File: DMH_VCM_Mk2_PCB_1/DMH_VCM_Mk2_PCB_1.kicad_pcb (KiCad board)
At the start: 2 copper layers, 48 x 175 mm, 88 parts, among them J1 TS_Jack_6.35mm_Sw, J10 TS_Jack_6.35mm_Sw, J100 IDC_02x05, J2 TS_Jack_6.35mm_Sw, J200 IDC_02x05, J3 TS_Jack_6.35mm_Sw, J4 TS_Jack_6.35mm_Sw, J5 TS_Jack_6.35mm_Sw, J50 Conn_01x06, J6 TS_Jack_6.35mm_Sw, J60 Conn_01x06, J7 TS_Jack_6.35mm_Sw, J70 Conn_01x06, J8 TS_Jack_6.35mm_Sw, J9 TS_Jack_6.35mm_Sw, Q1 BC548, Q2 BC548, Q3 BC548, Q4 BC548, Q5 BC548, Q6 BC548, U1 TL074, U2 TL074

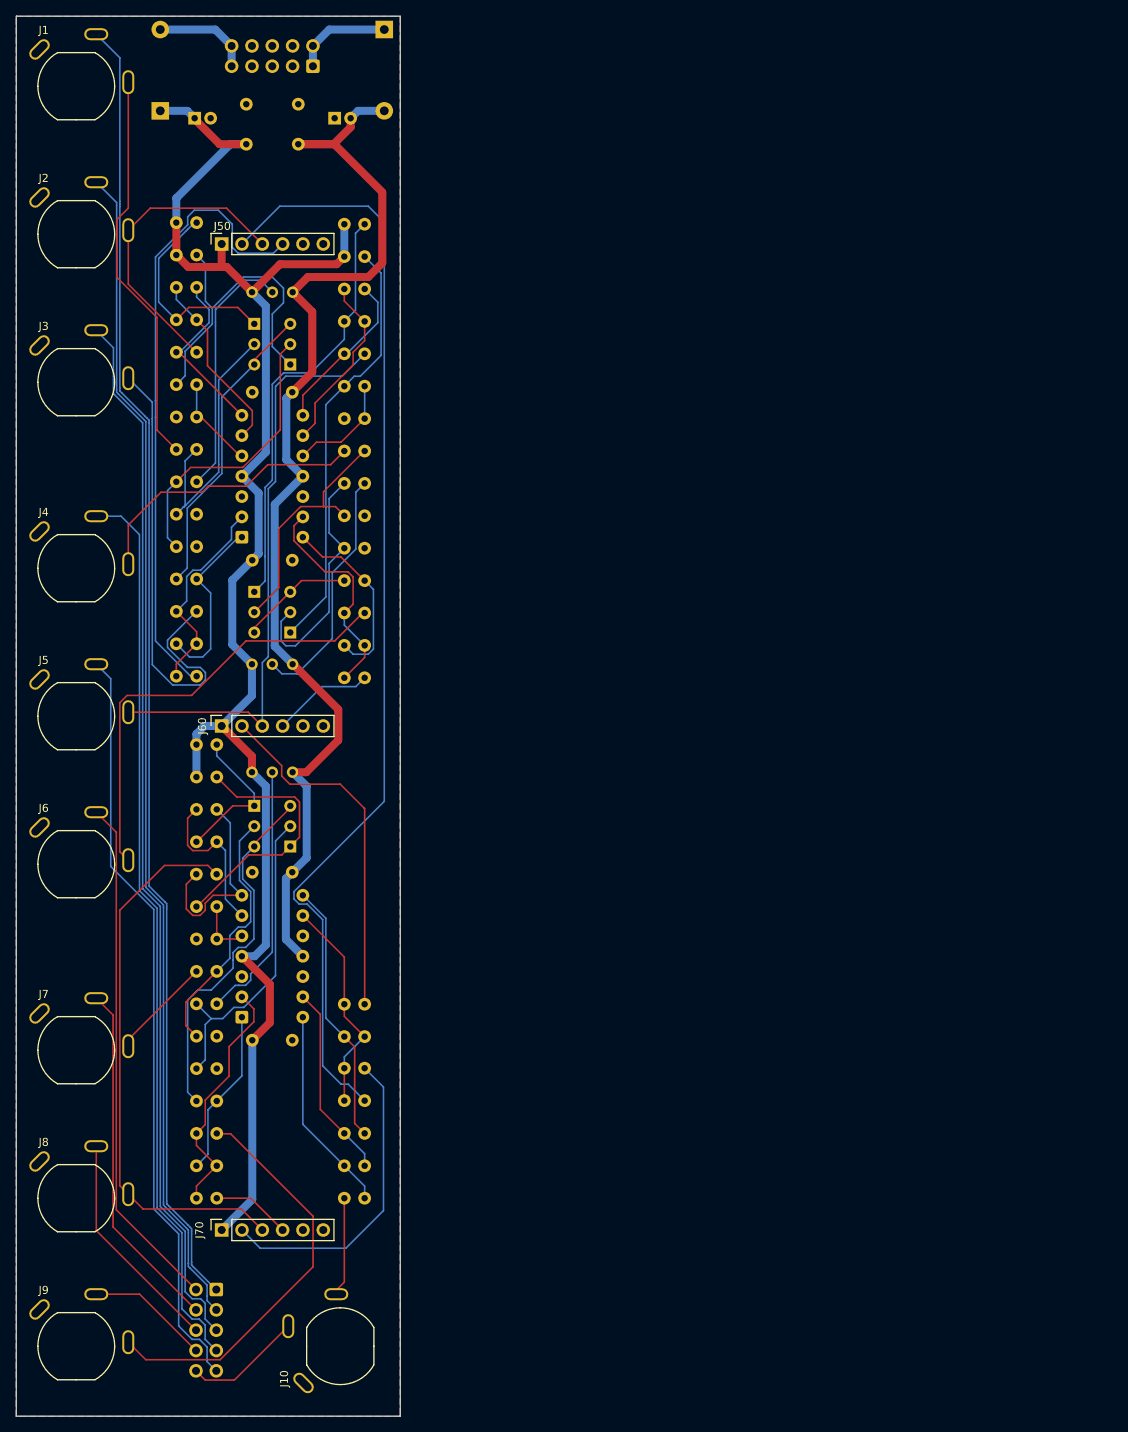
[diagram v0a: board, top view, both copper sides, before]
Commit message: PCB 1 placement in progress
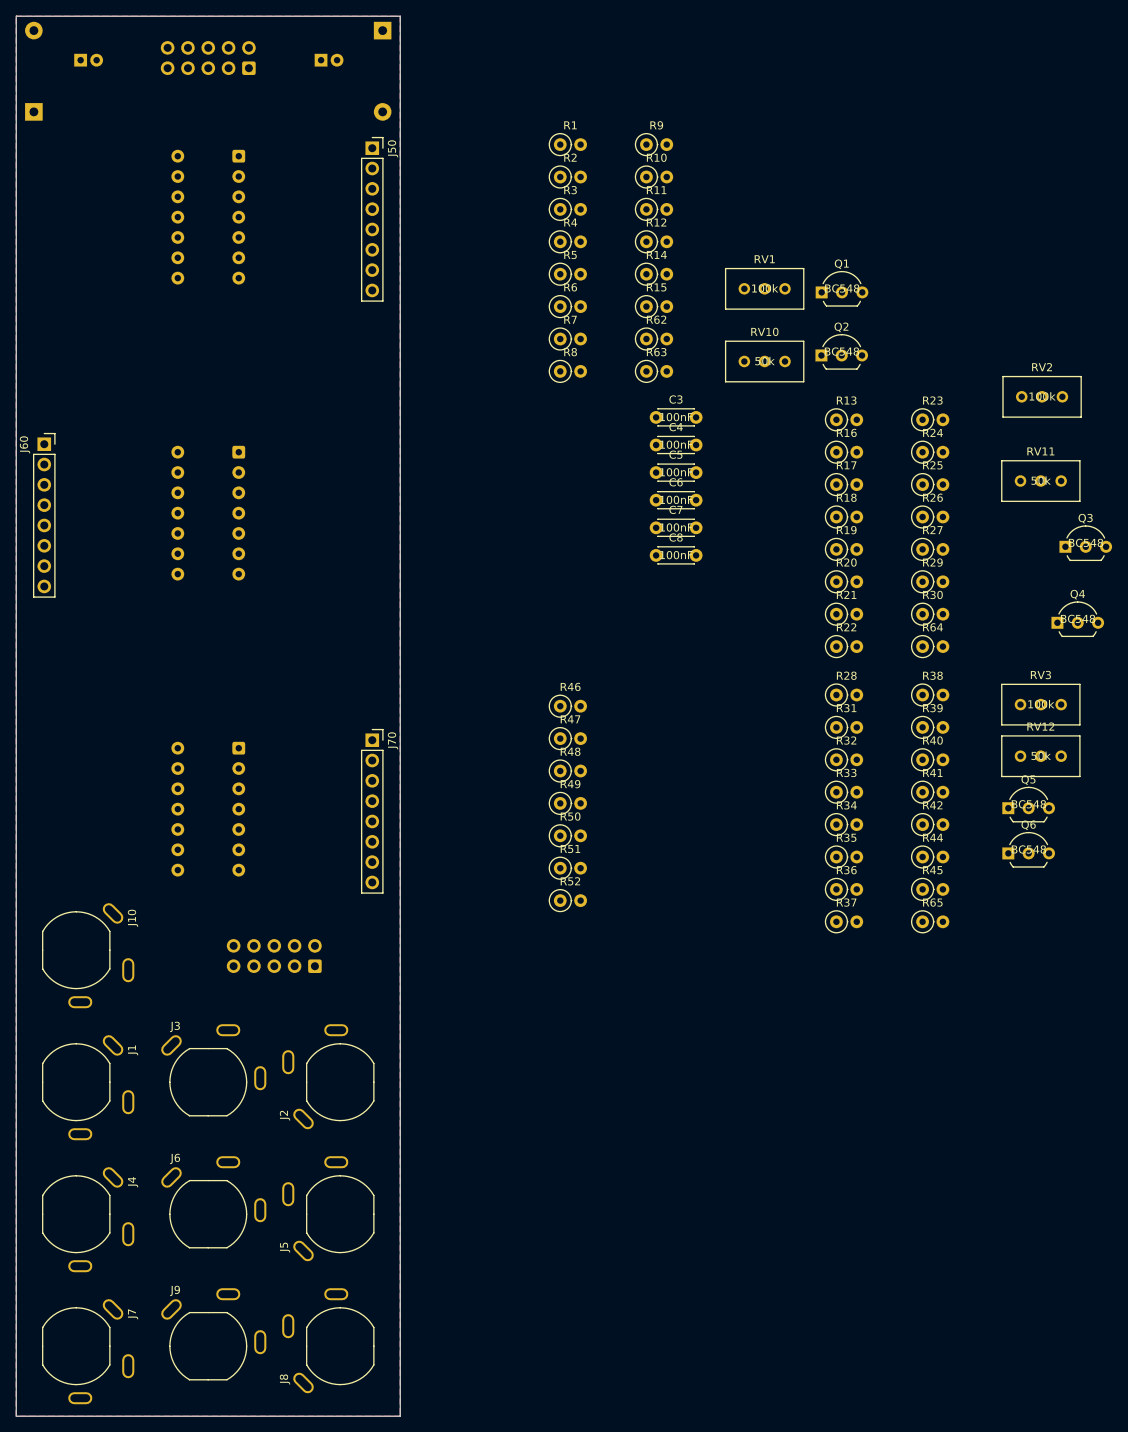
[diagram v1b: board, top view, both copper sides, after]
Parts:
- removed R43: 100k, Resistor_THT:R_Axial_DIN0207_L6.3mm_D2.5mm_P2.54mm_Vertical
- added R62: 33k, Resistor_THT:R_Axial_DIN0207_L6.3mm_D2.5mm_P2.54mm_Vertical, F.Cu at (129.8, 82.8)
- added R63: 100k, Resistor_THT:R_Axial_DIN0207_L6.3mm_D2.5mm_P2.54mm_Vertical, F.Cu at (129.8, 86.9)
- added R64: 100k, Resistor_THT:R_Axial_DIN0207_L6.3mm_D2.5mm_P2.54mm_Vertical, F.Cu at (164.3, 121.3)
- added R65: 100k, Resistor_THT:R_Axial_DIN0207_L6.3mm_D2.5mm_P2.54mm_Vertical, F.Cu at (164.3, 155.7)
- added RV10: 50k, Potentiometer_THT:Potentiometer_Bourns_3296W_Vertical, F.Cu at (147.1, 85.7)
- added RV11: 50k, Potentiometer_THT:Potentiometer_Bourns_3296W_Vertical, F.Cu at (181.6, 100.6)
- added RV12: 50k, Potentiometer_THT:Potentiometer_Bourns_3296W_Vertical, F.Cu at (181.6, 135.0)
- added U3: TL074, Package_DIP:DIP-14_W7.62mm_Socket, B.Cu at (78.8, 134.0)
- C3, C4, C5, C6, C7, C8, Q1, Q2, Q3, Q4, Q5, Q6, R1, R10, R11, R12, R14, R15, R16, R17, R18, R19, R2, R20, R21, R22, R23, R24, R25, R26, R27, R29, R3, R30, R31, R32, R33, R34, R35, R36, R37, R38, R39, R4, R40, R41, R42, R44, R45, R46, R47, R48, R49, R5, R50, R51, R52, R6, R7, R8, R9, RV1, RV2, RV3: moved to F.Cu
- J50, J60, J70: value Conn_01x06 -> Conn_01x08; footprint Connector_PinSocket_2.54mm:PinSocket_1x06_P2.54mm_Vertical -> Connector_PinSocket_2.54mm:PinSocket_1x08_P2.54mm_Vertical
- R13, R28: value 100k -> 33k; moved to F.Cu
- moved J1 124.5 mm to (58.5, 175.8), turned to -90 degrees
- moved J2 111.0 mm to (91.5, 175.8), turned to 90 degrees
- moved RV2 101.9 mm to (181.8, 90.1)
- moved Q3 101.6 mm to (182.1, 108.8), turned to 0 degrees
- moved RV3 96.4 mm to (181.6, 128.6)
- moved R44 96.3 mm to (164.3, 147.6), turned to 0 degrees
- moved R45 96.3 mm to (164.3, 151.7), turned to 0 degrees
- moved Q4 95.9 mm to (181.1, 118.3), turned to 0 degrees
- moved R38 94.8 mm to (164.3, 127.3), turned to 0 degrees
- moved R39 94.8 mm to (164.3, 131.4), turned to 0 degrees
- moved R40 94.8 mm to (164.3, 135.4), turned to 0 degrees
- moved R41 94.8 mm to (164.3, 139.5), turned to 0 degrees
- moved R42 94.8 mm to (164.3, 143.6), turned to 0 degrees
- moved Q5 94.3 mm to (175.0, 141.5), turned to 0 degrees
- moved Q6 89.8 mm to (175.0, 147.2), turned to 0 degrees
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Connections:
- J50 pad 5: GND -> /Inputs and Outputs/CV Amt A Pot
- J50 pad 6: GND -> /Inputs and Outputs/CV A Jack
- J60 pad 5: GND -> /Inputs and Outputs/CV Amt B Pot
- J60 pad 6: GND -> /Inputs and Outputs/CV B Jack
- J70 pad 5: GND -> /Inputs and Outputs/CV Amt C Pot
- J70 pad 6: GND -> /Inputs and Outputs/CV C Jack
- R13 pad 1: /Inputs and Outputs/CV A Jack -> /Inputs and Outputs/CV B Jack
- R13 pad 2: Net-(U1A--) -> Net-(U2D--)
- R18 pad 2: Net-(U1C--) -> Net-(U2A--)
- R19 pad 1: Net-(U1C--) -> Net-(U2A--)
- R21 pad 1: Net-(U1C-+) -> Net-(U2A-+)
- R22 pad 1: Net-(U1C-+) -> Net-(U2A-+)
- R28 pad 1: /Inputs and Outputs/CV B Jack -> /Inputs and Outputs/CV C Jack
- R28 pad 2: Net-(U1D--) -> Net-(U3A--)
- R29 pad 1: Net-(U1D--) -> Net-(U1C--)
- R3 pad 2: Net-(U1B--) -> Net-(U1D--)
- R30 pad 2: Net-(U1D--) -> Net-(U1C--)
- R33 pad 2: Net-(U2B--) -> Net-(U3B--)
- R34 pad 1: Net-(U2B--) -> Net-(U3B--)
- R36 pad 1: Net-(U2B-+) -> Net-(U3B-+)
- R37 pad 1: Net-(U2B-+) -> Net-(U3B-+)
- R4 pad 1: Net-(U1B--) -> Net-(U1D--)
- R44 pad 1: Net-(U2A--) -> Net-(U2B--)
- R45 pad 2: Net-(U2A--) -> Net-(U2B--)
- R46 pad 2: Net-(U2C--) -> Net-(U3D--)
- R47 pad 1: Net-(U2C--) -> Net-(U3D--)
- R48 pad 2: Net-(U2C--) -> Net-(U3D--)
- R49 pad 2: Net-(U2C--) -> Net-(U3D--)
- R50 pad 2: Net-(U2D--) -> Net-(U3C--)
- R51 pad 1: Net-(U2D--) -> Net-(U3C--)
- R6 pad 1: Net-(U1B-+) -> Net-(U1D-+)
- R7 pad 1: Net-(U1B-+) -> Net-(U1D-+)
- U1 pad 10: Net-(U1C-+) -> GND
- U1 pad 12: GND -> Net-(U1D-+)
- U1 pad 14: Net-(R27-Pad1) -> Net-(R3-Pad1)
- U1 pad 5: Net-(U1B-+) -> /Inputs and Outputs/CV Amt A Pot
- U1 pad 7: Net-(R3-Pad1) -> Net-(R63-Pad1)
- U1 pad 8: Net-(R18-Pad1) -> Net-(R27-Pad1)
- U2 pad 1: Net-(R42-Pad1) -> Net-(R18-Pad1)
- U2 pad 12: GND -> /Inputs and Outputs/CV Amt B Pot
- U2 pad 14: Net-(R51-Pad2) -> Net-(R64-Pad1)
- U2 pad 3: GND -> Net-(U2A-+)
- U2 pad 5: Net-(U2B-+) -> GND
- U2 pad 7: Net-(R33-Pad1) -> Net-(R42-Pad1)
- U2 pad 8: Net-(R47-Pad2) -> Net-(U2C--)
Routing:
- net +12V: track 204.9 -> 0.00 mm
- net Net-(J200-Pin_1): track 163.2 -> 0.00 mm
- net Net-(J200-Pin_2): track 147.2 -> 0.00 mm
- net -12V: track 144.7 -> 0.00 mm
- net /Inputs and Outputs/Mute A Switch: track 139.8 -> 0.00 mm
- net Net-(J200-Pin_3): track 131.8 -> 0.00 mm
- net Net-(J200-Pin_4): track 112.8 -> 0.00 mm
- net Net-(J200-Pin_5): track 95.1 -> 0.00 mm
- net /Inputs and Outputs/Offset A Pot: track 78.3 -> 0.00 mm
- net /Inputs and Outputs/Output B Jack: track 73.4 -> 0.00 mm
- net /Inputs and Outputs/Output C Jack: track 69.4 -> 0.00 mm
- net Net-(J200-Pin_6): track 64.8 -> 0.00 mm
- net /Inputs and Outputs/CV A Jack: track 58.0 -> 0.00 mm
- net /Inputs and Outputs/CV B Jack: track 55.4 -> 0.00 mm
- net Net-(Q3-C): track 53.7 -> 0.00 mm
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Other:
- board text added: "Mk2.0 - Month 2025"
- board text removed: "Mk1.1 - March 2025"

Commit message: PCB 1 placement done
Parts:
- C3, C4, C5, C6, C7, C8, Q1, Q2, Q3, Q4, Q5, Q6, R1, R10, R11, R12, R13, R14, R15, R16, R17, R18, R19, R2, R20, R21, R22, R23, R24, R25, R26, R27, R28, R29, R3, R30, R31, R32, R33, R34, R35, R36, R37, R38, R39, R4, R40, R41, R42, R44, R45, R46, R47, R48, R49, R5, R50, R51, R52, R6, R62, R63, R64, R65, R7, R8, R9, RV1, RV10, RV11, RV12, RV2, RV3: moved to B.Cu
- moved RV3 117.9 mm to (63.7, 129.5), turned to 180 degrees
- moved RV2 116.3 mm to (65.5, 92.5)
- moved RV11 116.1 mm to (65.5, 98.0)
- moved R64 102.5 mm to (69.8, 81.5), turned to 180 degrees
- moved R30 102.1 mm to (69.8, 78.5), turned to 180 degrees
- moved Q2 101.4 mm to (52.7, 62.8)
- moved R29 100.8 mm to (67.7, 84.5)
- moved R27 99.0 mm to (67.7, 87.5)
- moved RV12 98.5 mm to (83.2, 129.8), turned to -90 degrees
- moved Q1 95.6 mm to (57.8, 59.0), turned to 180 degrees
- moved R65 95.1 mm to (82.7, 106.8)
- moved R45 91.7 mm to (82.7, 109.8)
- moved Q4 90.7 mm to (92.2, 100.7)
- moved R44 88.7 mm to (82.7, 112.8)
- moved R42 86.2 mm to (82.7, 115.8)
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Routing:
- net Net-(D2-K): track 0.00 -> 17.6 mm
- net Net-(D1-A): track 0.00 -> 17.6 mm

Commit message: PCB 1 routine in progress
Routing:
- net +12V: track 0.00 -> 202.2 mm
- net -12V: track 0.00 -> 157.2 mm
- net /Inputs and Outputs/Mute A Switch: track 0.00 -> 155.9 mm
- net /Inputs and Outputs/CV B Jack: track 0.00 -> 152.4 mm
- net /Inputs and Outputs/Output A Jack: track 0.00 -> 144.0 mm
- net /Inputs and Outputs/Input B Jack: track 0.00 -> 119.8 mm
- net /Inputs and Outputs/Input A Jack: track 0.00 -> 113.9 mm
- net Net-(Q1-B): track 0.00 -> 54.3 mm
- net Net-(Q3-E): track 0.00 -> 53.6 mm
- net /Inputs and Outputs/Mute C Switch: track 0.00 -> 44.4 mm
- net /Inputs and Outputs/Output B Jack: track 0.00 -> 43.8 mm
- net Net-(U2A-+): track 0.00 -> 43.6 mm
- net Net-(R24-Pad1): track 0.00 -> 43.0 mm
- net Net-(Q1-E): track 0.00 -> 42.5 mm
- net Net-(Q2-B): track 0.00 -> 40.0 mm
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
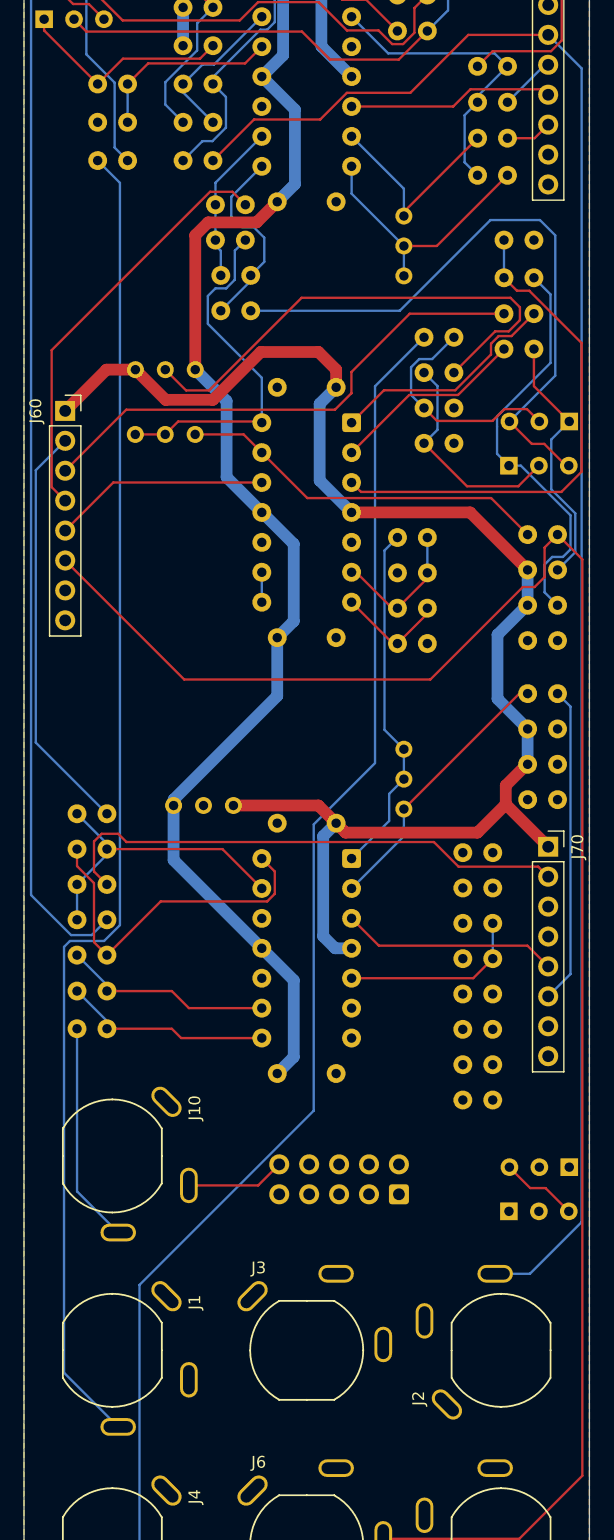
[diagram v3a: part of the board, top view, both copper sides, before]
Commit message: PCB 1 routing still in progress
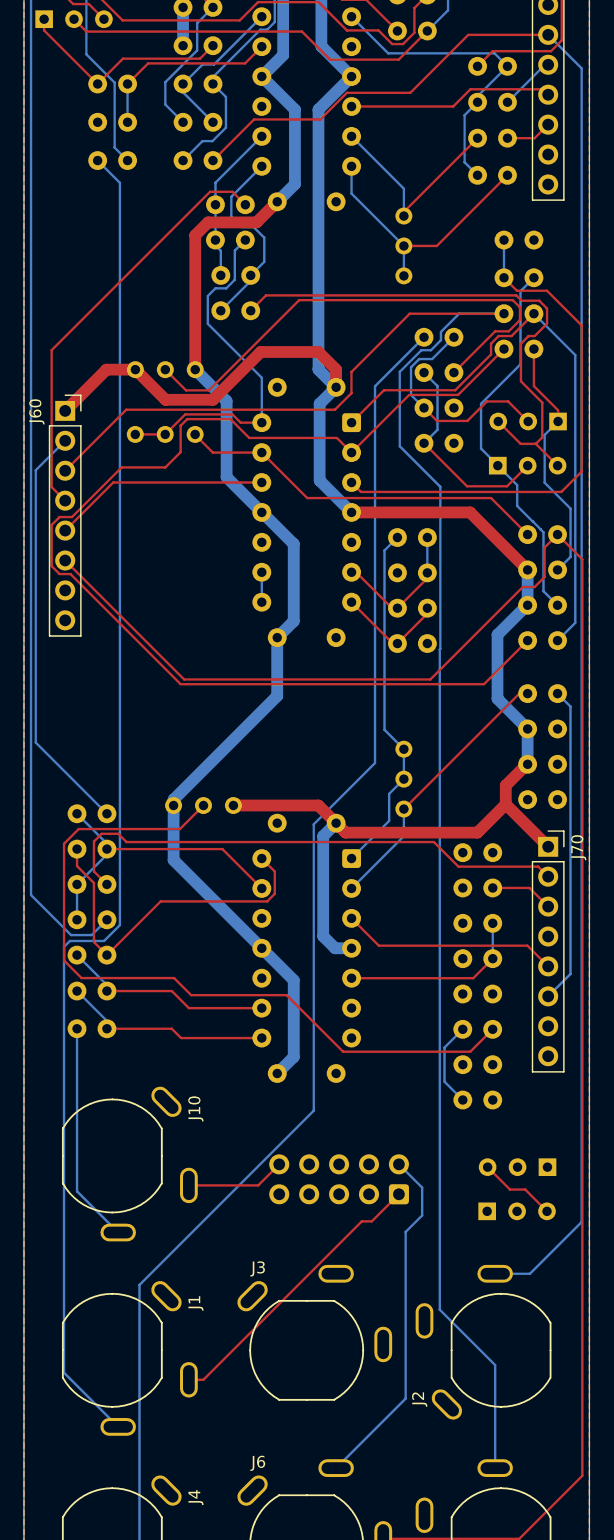
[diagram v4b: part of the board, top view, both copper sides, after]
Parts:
- moved Q5 1.85 mm to (95.4, 160.2)
- moved Q6 1.85 mm to (90.3, 163.9)
- moved Q3 0.95 mm to (96.3, 96.9)
- moved Q4 0.95 mm to (91.2, 100.7)
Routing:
- net /Inputs and Outputs/Output B Jack: track 43.8 -> 151.6 mm
- net Net-(U2A--): track 16.6 -> 97.8 mm
- net Net-(R39-Pad1): track 0.00 -> 63.5 mm
- net Net-(R18-Pad1): track 19.8 -> 49.7 mm
- net Net-(J200-Pin_6): track 0.00 -> 29.6 mm
- net +12V: track 202.2 -> 230.3 mm
- net Net-(J200-Pin_1): track 0.00 -> 24.4 mm
- net Net-(Q6-B): track 0.00 -> 7.29 mm
- net Net-(Q3-E): track 53.6 -> 46.4 mm
- net /Inputs and Outputs/Output C Jack: track 0.00 -> 5.36 mm
- net Net-(Q4-C): track 35.3 -> 32.4 mm
- net Net-(Q4-B): track 18.9 -> 18.0 mm
- net Net-(U2A-+): track 43.6 -> 44.5 mm
- net Net-(Q3-C): track 22.1 -> 21.4 mm

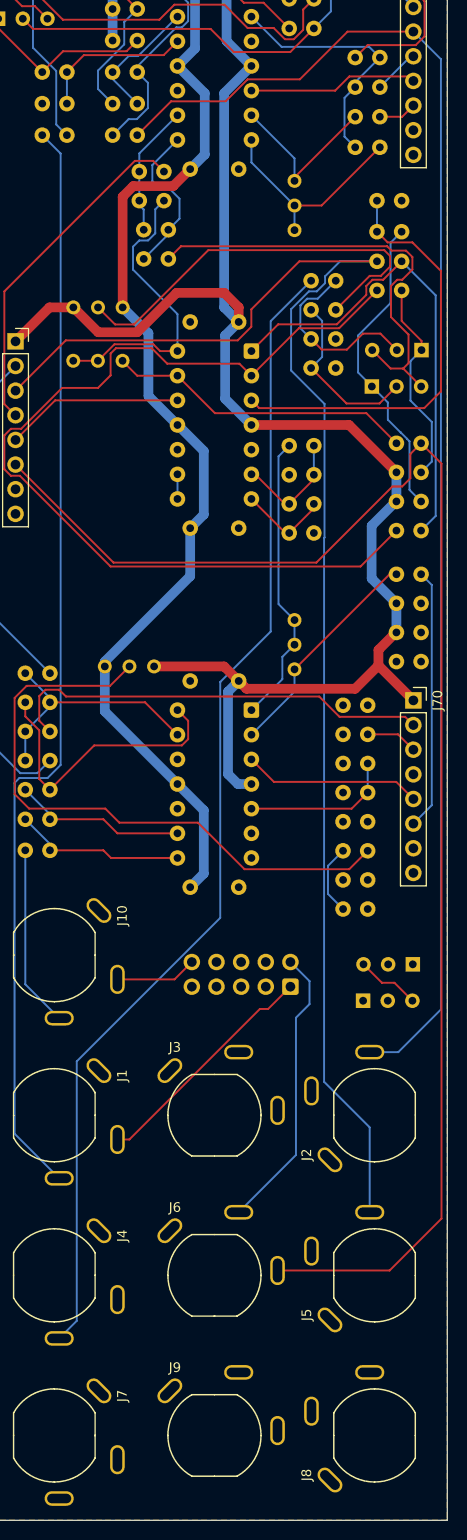
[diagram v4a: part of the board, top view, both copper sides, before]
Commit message: Completed PCB 1 routing
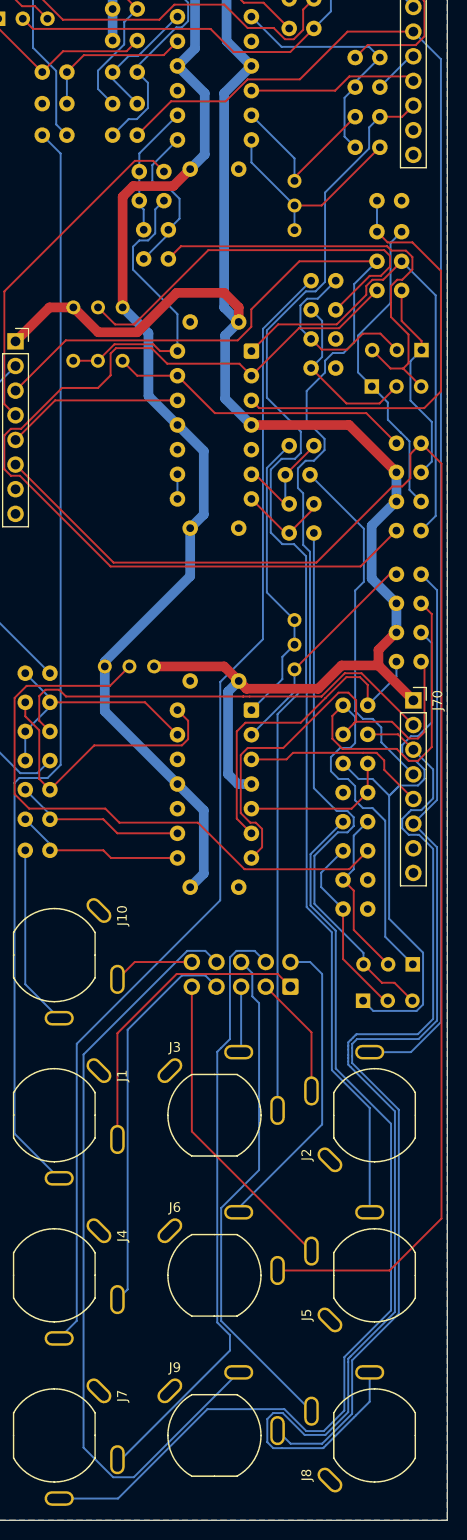
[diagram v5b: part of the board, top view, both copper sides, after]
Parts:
- moved R45 2.14 mm to (84.8, 109.8), turned to 180 degrees
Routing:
- net /Inputs and Outputs/CV A Jack: track 3.93 -> 118.7 mm
- net /Inputs and Outputs/Output C Jack: track 5.36 -> 118.4 mm
- net /Inputs and Outputs/Input C Jack: track 0.00 -> 102.5 mm
- net /Inputs and Outputs/CV C Jack: track 26.9 -> 110.1 mm
- net Net-(J200-Pin_9): track 0.00 -> 80.8 mm
- net Net-(Q5-C): track 0.00 -> 64.5 mm
- net Net-(J200-Pin_7): track 0.00 -> 62.3 mm
- net Net-(Q6-C): track 0.00 -> 60.4 mm
- net Net-(J200-Pin_8): track 0.00 -> 52.5 mm
- net Net-(Q5-E): track 6.59 -> 57.7 mm
- net Net-(R33-Pad1): track 0.00 -> 47.0 mm
- net Net-(J200-Pin_4): track 0.00 -> 40.2 mm
- net /Inputs and Outputs/Offset C Pot: track 0.00 -> 36.6 mm
- net Net-(U3B--): track 0.00 -> 35.1 mm
- net Net-(J200-Pin_5): track 0.00 -> 32.4 mm
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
